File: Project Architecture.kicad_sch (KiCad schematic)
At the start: 0 parts

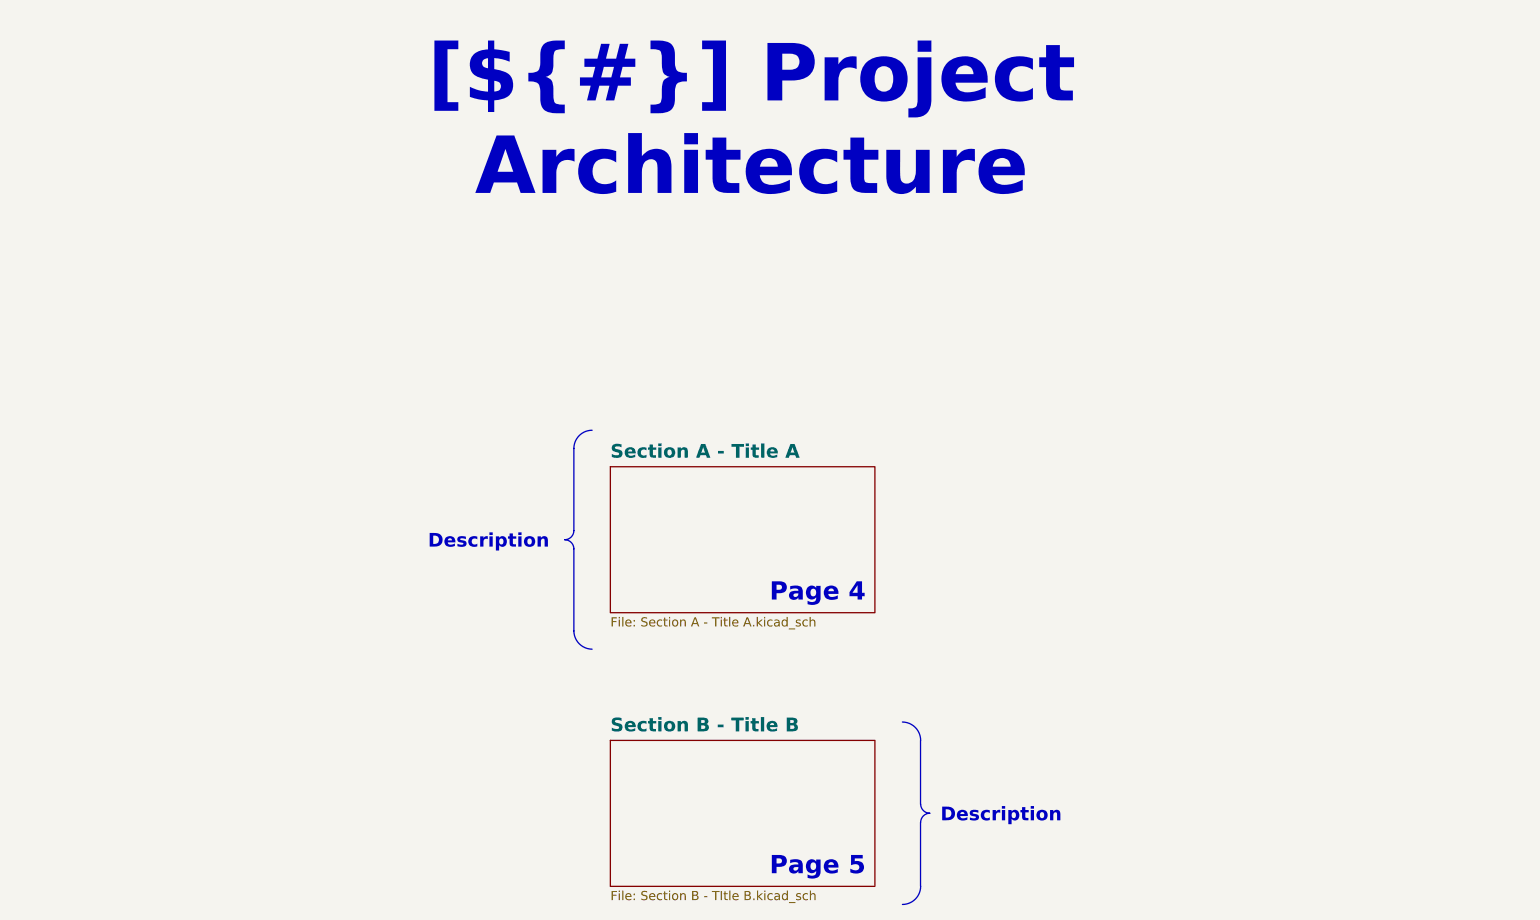
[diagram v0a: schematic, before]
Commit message: feat: Changed templates to be specific to Ryan Dynamics
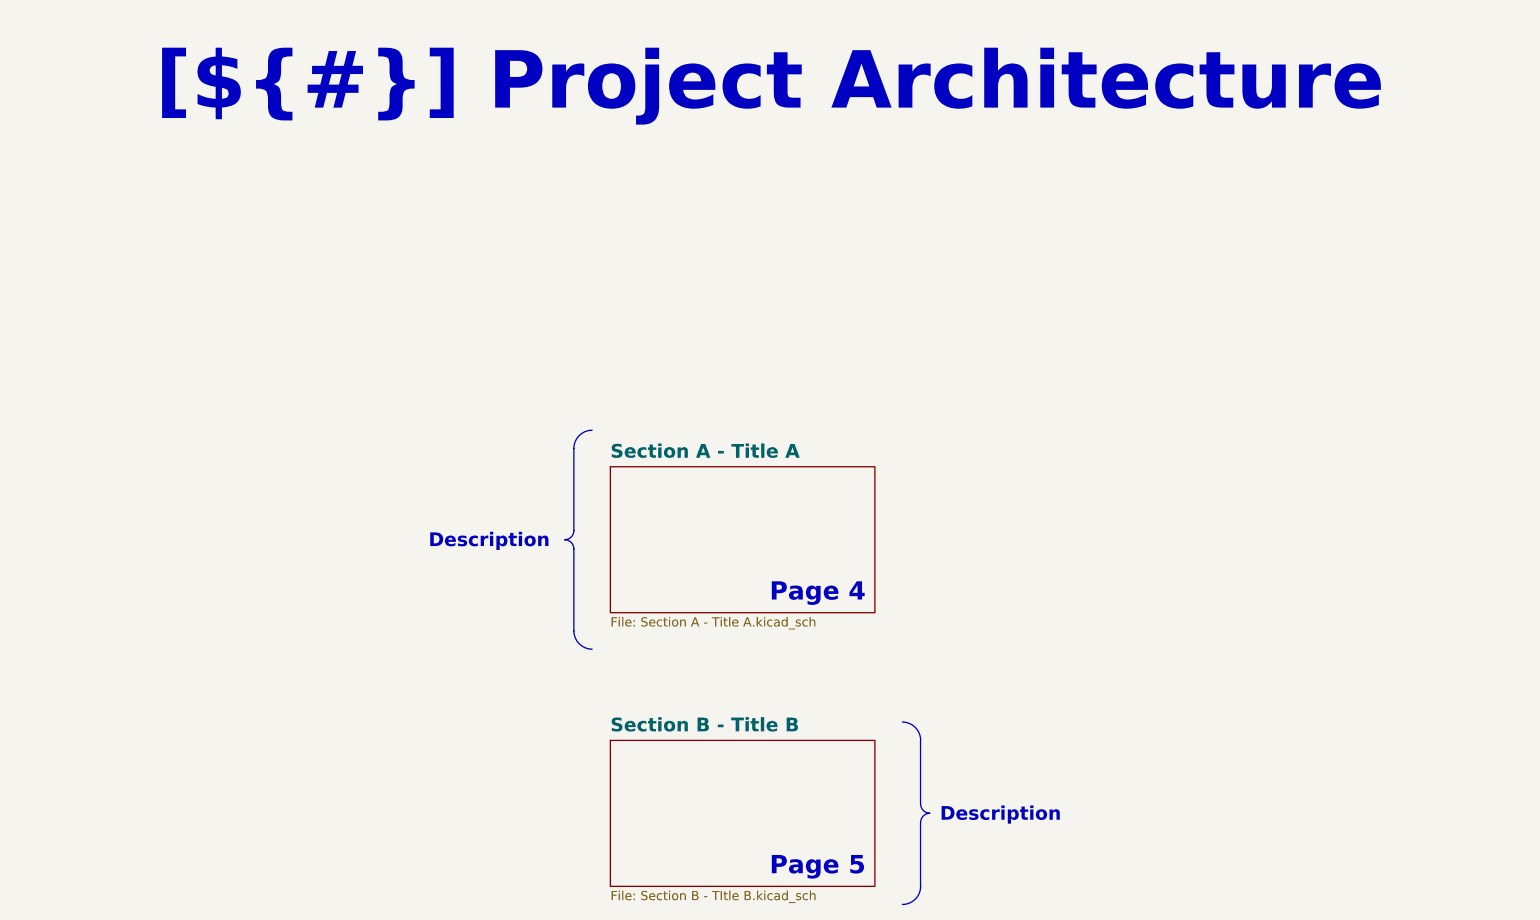
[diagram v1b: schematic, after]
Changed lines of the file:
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@@
 (kicad_sch
-	(version 20231120)
+	(version 20250114)
 	(generator "eeschema")
-	(generator_version "8.0")
+	(generator_version "9.0")
 	(paper "A3")
 	(title_block
@@
 		(company "${COMPANY}")
 	)
-	(polyline
-		(pts
-			(xy 185.42 87.63) (xy 185.42 99.06)
-		)
-		(stroke
-			(width 0)
-			(type default)
-		)
-	)
-	(polyline
-		(pts
-			(xy 233.68 125.73) (xy 233.68 134.62)
-		)
-		(stroke
-			(width 0)
-			(type default)
-		)
-	)
-	(polyline
-		(pts
-			(xy 185.42 85.09) (xy 185.42 73.66)
-		)
-		(stroke
-			(width 0)
-			(type default)
-		)
-	)
-	(polyline
-		(pts
-			(xy 233.68 114.3) (xy 233.68 123.19)
-		)
-		(stroke
-			(width 0)
-			(type default)
-		)
-	)
 	(arc
 		(start 185.42 85.09)
@@
 		)
 	)
+	(text "Page 5"
+		(exclude_from_sim no)
+		(at 226.06 133.35 0)
+		(effects
+			(font
+				(size 2.54 2.54)
+				(bold yes)
+				(color 100 70 50 1)
+			)
+			(justify right bottom)
+			(href "#5")
+		)
+	)
+	(text "Page 4"
+		(exclude_from_sim no)
+		(at 226.06 95.25 0)
+		(effects
+			(font
+				(size 2.54 2.54)
+				(bold yes)
+				(color 20 60 40 1)
+			)
+			(justify right bottom)
+			(href "#4")
+		)
+	)
 	(text_box "Description"
 		(exclude_from_sim no)
 		(at 166.37 83.82 0)
 		(size 17.145 5.08)
+		(margins 1.4287 1.4287 1.4287 1.4287)
 		(stroke
 			(width -0.0001)
@@
 		(at 234.95 121.92 0)
 		(size 26.015 5.1)
+		(margins 1.4287 1.4287 1.4287 1.4287)
 		(stroke
 			(width -0.0001)
@@
 	(text_box "[${#}] ${TITLE}"
 		(exclude_from_sim no)
-		(at 144.78 21.59 0)
-		(size 130.81 12.7)
+		(at 121.92 15 0)
+		(size 181.61 15)
+		(margins 5.9999 5.9999 5.9999 5.9999)
 		(stroke
 			(width -0.0001)
@@
 		(effects
 			(font
-				(face "Times New Roman")
 				(size 8 8)
 				(thickness 1.2)
@@
 		)
 	)
-	(text "Page 5"
-		(exclude_from_sim no)
-		(at 226.06 133.35 0)
-		(effects
-			(font
-				(size 2.54 2.54)
-				(bold yes)
-				(color 100 70 50 1)
-			)
-			(justify right bottom)
-			(href "#5")
-		)
-	)
-	(text "Page 4"
-		(exclude_from_sim no)
-		(at 226.06 95.25 0)
-		(effects
-			(font
-				(size 2.54 2.54)
-				(bold yes)
-				(color 20 60 40 1)
-			)
-			(justify right bottom)
-			(href "#4")
+	(polyline
+		(pts
+			(xy 185.42 87.63) (xy 185.42 99.06)
+		)
+		(stroke
+			(width 0)
+			(type default)
+		)
+	)
+	(polyline
+		(pts
+			(xy 233.68 125.73) (xy 233.68 134.62)
+		)
+		(stroke
+			(width 0)
+			(type default)
+		)
+	)
+	(polyline
+		(pts
+			(xy 185.42 85.09) (xy 185.42 73.66)
+		)
+		(stroke
+			(width 0)
+			(type default)
+		)
+	)
+	(polyline
+		(pts
+			(xy 233.68 114.3) (xy 233.68 123.19)
+		)
+		(stroke
+			(width 0)
+			(type default)
 		)
 	)
@@
 		(at 190.5 114.3)
 		(size 36.83 20.32)
+		(exclude_from_sim no)
+		(in_bom yes)
+		(on_board yes)
+		(dnp no)
 		(fields_autoplaced yes)
 		(stroke
@@
 		(at 190.5 76.2)
 		(size 36.83 20.32)
+		(exclude_from_sim no)
+		(in_bom yes)
+		(on_board yes)
+		(dnp no)
 		(fields_autoplaced yes)
 		(stroke
